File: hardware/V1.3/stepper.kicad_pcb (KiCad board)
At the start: 4 copper layers, 40 x 40 mm, 231 parts, among them J1 DRILL, J101 USB-MINI-B-SMD, J102 DRILL, J103 DRILL, J104 DRILL, J105 DRILL, J2 DRILL, J3 DRILL, J4 DRILL, J401 STACK-UP-HIGH, J402 STACK-DOWN, J403 STACK-UP-HIGH, J404 STACK-DOWN, J5 USB-MINI-B-SMD, J6 STACK-UP-HIGH, J7 STACK-DOWN, J8 STACK-UP-HIGH, J9 STACK-DOWN, P1 black, P2 green, P201 black, P202 green, P3 CON-SENSOR, P301 CON-SENSOR, P302 CON-SENSOR, P4 CON-SENSOR, Q1 FDS8449, Q2 AO4421, Q201 FDS8449, Q202 AO4421, Q203 2N7002, Q3 2N7002, SW1 Reset, SW101 Reset, SW102 Erase, SW2 Erase, U1 AT91SAM3SXB, U101 AT91SAM3SXB, U102 82400152, U2 ZXCT1086, U201 ZXCT1086, U202 TMC21XX, U3 DRV8811PWP, U4 EUP3406, U501 EUP3406, X1 16Mhz, X101 16Mhz

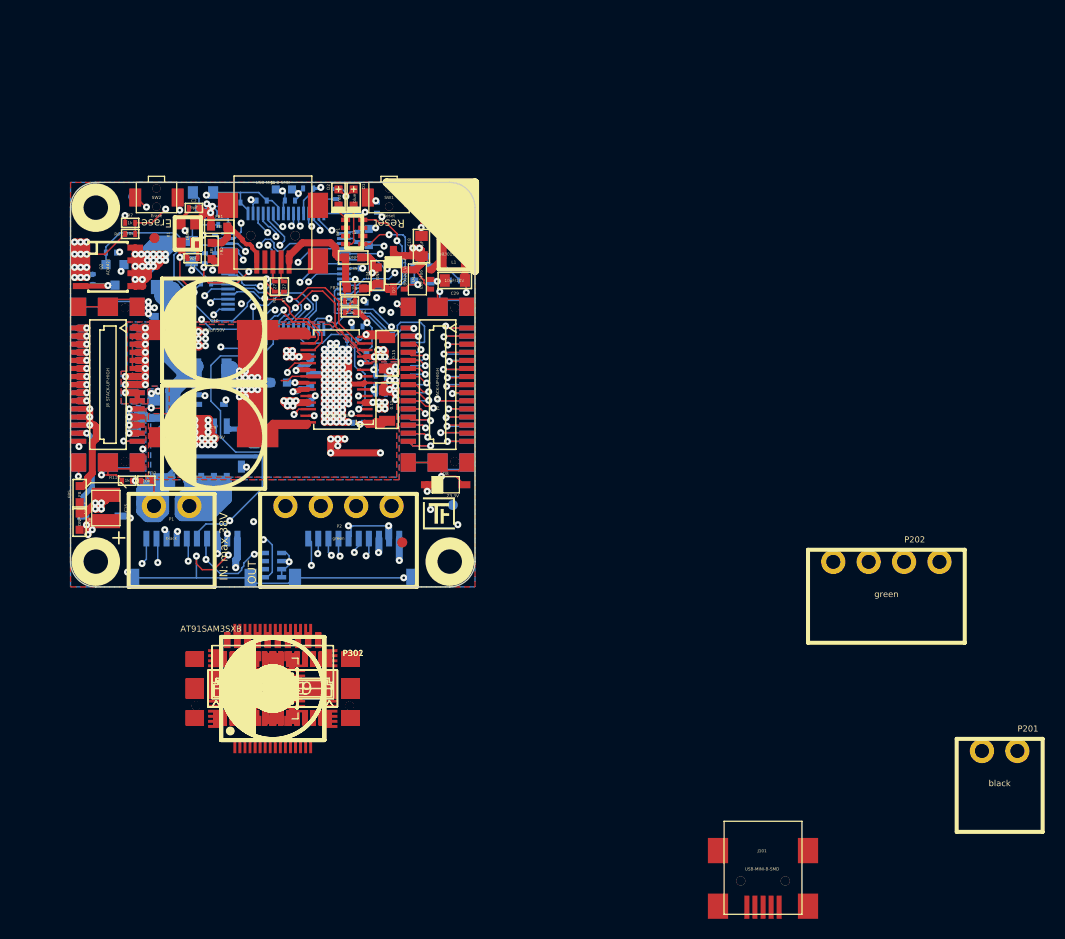
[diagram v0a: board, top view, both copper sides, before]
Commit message: remove old parts, place important components to pcb
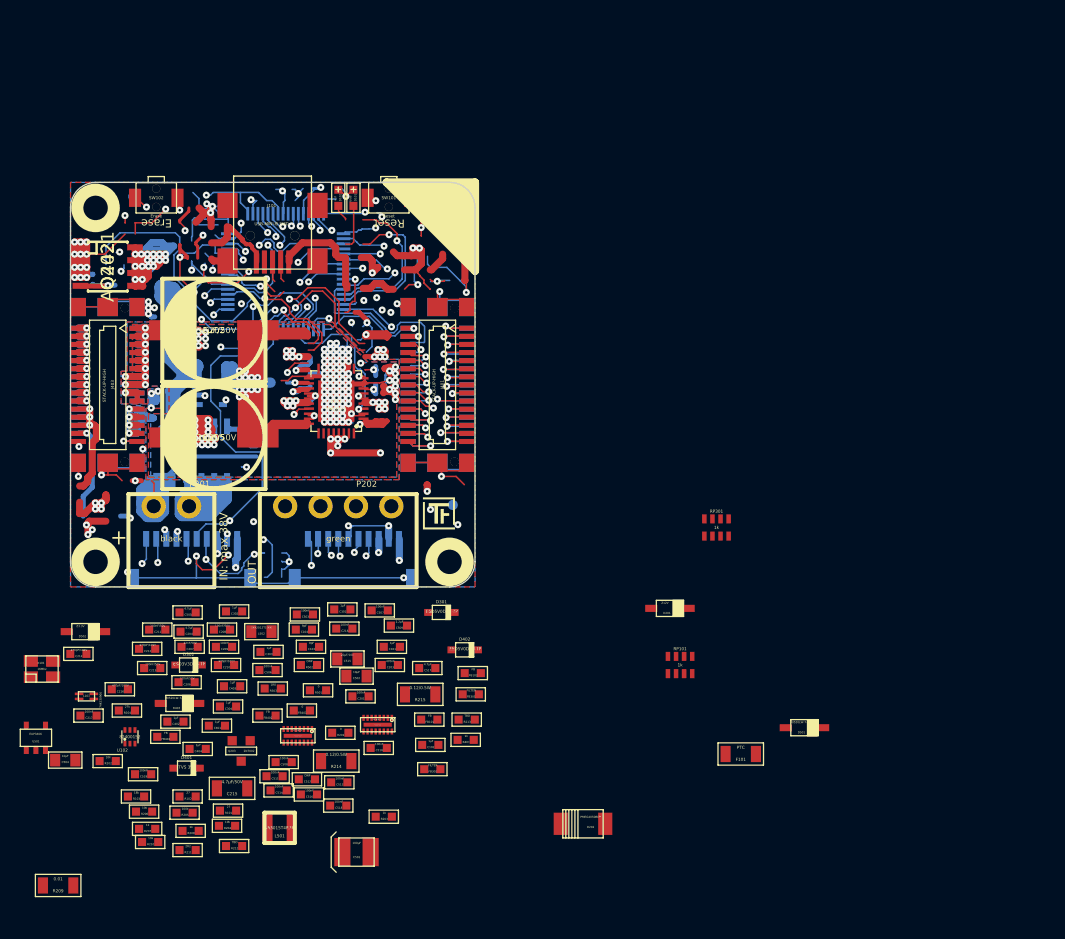
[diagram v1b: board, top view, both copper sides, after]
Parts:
- removed C1, C2: 9pF, 0402
- removed C10, C9: 330µF/50V, ELKO_103
- removed C11, C14, C17, C20, C21, C22, C24, C25, C27, C28, C3, C30, C32, C33, C4, C5: 100nF, 0402
- removed C12, C13, C7: 220nF, 0603
- removed C15: 100µF, 3528-21
- removed C16, C18: 10µF, 0805
- removed C19, C31: 4.7µF, 0603
- removed C23: 2.2µF, 0603
- removed C26: DNP, 0402
- removed C29: 10µF/10V, 0805
- removed C34, C35, C36, R24: DNP, 0603
- removed C6, C8: 1nF, 0402
- removed D1: blue, D0603
- removed D2: red, D0603
- removed D3: Z12V, SOD-123
- removed D4, D5: PMEG4050BEP, SOD-128
- removed D6, D7: B0520LW-7-F, SOD-123
- removed D8: Z3.3V, SOD-123
- removed FB1, FB2, FB3, FB4, FB5, R5: FB, 0603
- removed the Fiducial_Mark at (135.0, 78.3)
- removed the Fiducial_Mark at (159.5, 108.4)
- removed J1, J2, J3, J4: DRILL, DRILL_NP
- removed J5: USB-MINI-B-SMD, USB-MINI-B-SMD
- removed J6, J8: STACK-UP-HIGH, BTB08-ACS-TOP
- removed J7, J9: STACK-DOWN, BTB08-ACS-BTM
- removed L1: NR3015T4R7M, NR3030
- removed L2: LBR2012T100K, 0805
- removed P1: black, OQ_2P
- removed P2: green, OQ_4P
- removed P3, P4: CON-SENSOR, CON-SENSOR
- removed Q1: FDS8449, SOIC-8-MOSFET
- removed Q2: AO4421, SOIC-8-MOSFET
- removed Q3: 2N7002, SOT23GDS
- removed R1, R2: 27, 0402
- removed R10, R12, R18, R6, R8: 10k, 0402
- removed R11, R13, R16, R22, R7: 1k, 0402
- removed R14, R4: 2.7k, 0402
- removed R15, R19: 47k, 0402
- removed R17: 0.01, 1206
- removed R20, R21: 0.15, 1206
- removed R23: 0, 0603
- removed R25: 1R0, 0402
- removed R3: 1.8k, 0402
- removed R9: 100k, 0402
- removed RP1, RP2: 1k, 4X0603
- removed SW1: Reset, TACT-SWITCH
- removed SW2: Erase, TACT-SWITCH
- removed U1: AT91SAM3SXB, LQFP64
- removed U2: ZXCT1086, SOT23-5
- removed U3: DRV8811PWP, HTSSOP28
- removed U4: EUP3406, SOT23-5
- removed X1: 16Mhz, CRYSTAL_3225
- C103, C104, C503, C506, C507, C508, C510, C511, C512, C513, C514, C516, C518, C519, R101, R102, R103, R104, R202, R203, R204, R205, R206, R207, R208, R210, R211, R212, R213, R401, R503: footprint kicad-libraries:0402 -> kicad-libraries:0603
- D203, J402, J404, P301, P302, Q201, U101, U201: moved to B.Cu
- moved P201 85.4 mm to (136.7, 104.8)
- moved J101 80.1 mm to (146.7, 72.8)
- moved P202 54.5 mm to (153.2, 104.8)
- moved D501 52.7 mm to (199.3, 126.7)
- moved J104 50.7 mm to (129.2, 75.3)
- moved J103 50.6 mm to (164.2, 75.3)
- moved SW102 49.9 mm to (135.2, 74.3)
- moved SW101 49.9 mm to (158.2, 74.3)
- moved D101 49.2 mm to (154.7, 74.3), turned to 270 degrees
- moved D102 49.0 mm to (153.2, 74.3), turned to 270 degrees
- moved F101 46.7 mm to (193.0, 129.3)
- moved RP301 46.7 mm to (190.6, 106.9)
- moved Q202 44.8 mm to (130.4, 81.1), turned to 270 degrees
- moved U101 41.2 mm to (148.0, 81.6)
- moved RP101 40.3 mm to (187.0, 120.5)
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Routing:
- net VSTACK: track 99.9 -> 0.00 mm, vias 8 -> 0
- net Net-(C303-Pad1): track 0.00 -> 99.9 mm, vias 0 -> 8
- net N-000105: track 87.2 -> 0.00 mm, vias 5 -> 0
- net Net-(C212-Pad2): track 0.00 -> 87.2 mm, vias 0 -> 5
- net VPP: track 78.3 -> 0.00 mm, vias 16 -> 0
- net Net-(C202-Pad1): track 0.00 -> 78.3 mm, vias 0 -> 16
- net Net-(C210-Pad2): track 0.00 -> 74.5 mm, vias 0 -> 5
- net N-000108: track 74.5 -> 0.00 mm, vias 5 -> 0
- net (no net): track 0.00 -> 71.9 mm, vias 0 -> 14
- net Net-(FILTER302-Pad7): track 0.00 -> 62.1 mm, vias 0 -> 1
- net BRICKLET-IO1_3: track 75.9 -> 13.8 mm, vias 2 -> 1
- net Net-(C214-Pad2): track 0.00 -> 61.8 mm, vias 0 -> 5
- net N-000100: track 61.8 -> 0.00 mm, vias 5 -> 0
- net BRICKLET-I2C-SCL: track 83.6 -> 23.6 mm, vias 4 -> 2
- net Net-(FILTER301-Pad1): track 0.00 -> 57.3 mm, vias 0 -> 1
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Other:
- board text added: "1.3"
- board text removed: "1.2"

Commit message: change step down to ldo, pcb: partially placement
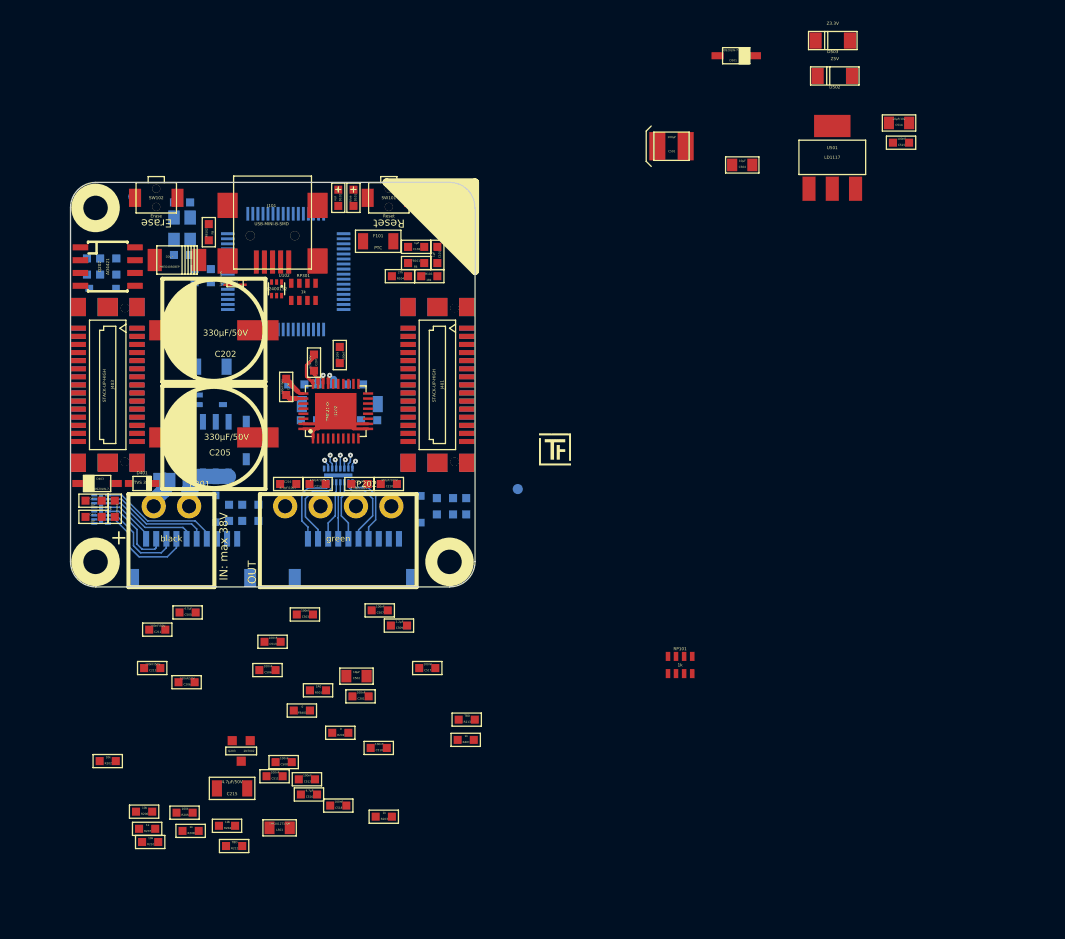
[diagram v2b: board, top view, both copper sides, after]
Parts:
- removed C519: 100nF, kicad-libraries:0603
- removed L502: LBR2012T100K, kicad-libraries:0805
- removed R502: DNP, kicad-libraries:0603
- removed R503: 1R0, kicad-libraries:0603
- added D503: Z3.3V, kicad-libraries:MiniMelf, F.Cu at (202.1, 58.8)
- C103, C104, C203, C204, C217, C218, C301, C302, C303, C304, C402, C404, D201, D301, D302, D402, FB301, FB302, FB403, FILTER301, FILTER302, R101, R102, R209, R211, R214, R215, X101: moved to B.Cu
- C512: value DNP -> 100nF
- C514: value 100nF -> 10µF/10V; footprint kicad-libraries:0603 -> kicad-libraries:0805
- C515: value 10µF/10V -> 100nF; footprint kicad-libraries:0805 -> kicad-libraries:0603
- C516: value 100nF -> 4.7µF
- C517: value 4.7µF -> 100nF
- D502: value Z3.3V -> Z5V; footprint kicad-libraries:SOD-123 -> kicad-libraries:MiniMelf
- L501: value NR3015T4R7M -> LBR2012T100K; footprint kicad-libraries:NR3030 -> kicad-libraries:0805
- R501: value 0 -> 1R0
- U501: value EUP3406 -> LD1117; footprint kicad-libraries:SOT23-5 -> kicad-libraries:SOT-223
- moved U501 97.4 mm to (202.1, 70.3)
- moved D502 92.3 mm to (202.3, 62.2)
- moved C514 90.1 mm to (208.7, 66.9)
- moved C504 89.1 mm to (193.2, 71.0)
- moved C501 76.4 mm to (186.2, 69.2)
- moved C515 74.9 mm to (208.8, 68.8)
- moved D202 68.7 mm to (137.2, 80.5), turned to 180 degrees
- moved D501 66.8 mm to (192.6, 60.2)
- moved F101 62.1 mm to (157.2, 78.6), turned to 180 degrees
- moved R103 59.1 mm to (162.2, 82.0), turned to 180 degrees
- moved R209 53.5 mm to (140.7, 91.0), turned to 180 degrees
- moved R101 52.3 mm to (139.8, 82.7)
- moved R102 52.2 mm to (139.8, 81.3)
- moved FB102 50.8 mm to (140.4, 77.7), turned to 270 degrees
- moved R104 50.7 mm to (159.3, 82.0)
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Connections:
- C512 pad 1: 3V3 -> Net-(C509-Pad1)
- C512 pad 2: Net-(C512-Pad2) -> GND
- C514 pad 1: Net-(C509-Pad1) -> 3V3
- C516 pad 1: 3V3 -> Net-(C516-Pad1)
- C518 pad 1: Net-(C518-Pad1) -> 3V3
- D502 pad 2: 3V3 -> VSTACK
- FILTER301 pad 10: BRICKLET-IO0_3 -> BRICKLET-IO0_0/AD0
- FILTER301 pad 11: BRICKLET-IO0_2/PWM0 -> BRICKLET-IO0_1
- FILTER301 pad 12: BRICKLET-IO0_1 -> BRICKLET-IO0_2/PWM0
- FILTER301 pad 13: BRICKLET-IO0_0/AD0 -> BRICKLET-IO0_3
- L501 pad 1: Net-(L501-Pad1) -> Net-(C509-Pad1)
- L501 pad 2: 3V3 -> Net-(C517-Pad1)
- P301 pad 10: Net-(FILTER301-Pad7) -> Net-(FILTER301-Pad4)
- P301 pad 7: Net-(FILTER301-Pad4) -> Net-(FILTER301-Pad7)
- P301 pad 8: Net-(FILTER301-Pad5) -> Net-(FILTER301-Pad6)
- P301 pad 9: Net-(FILTER301-Pad6) -> Net-(FILTER301-Pad5)
- R501 pad 1: 3V3 -> Net-(C516-Pad1)
- R501 pad 2: Net-(C512-Pad2) -> Net-(C517-Pad1)
- U101 pad 64: Net-(C518-Pad1) -> Net-(C517-Pad1)
- U102 pad 1: Net-(J101-Pad3) -> Net-(J101-Pad2)
- U102 pad 3: Net-(J101-Pad2) -> Net-(J101-Pad3)
- U102 pad 4: Net-(L101-Pad4) -> Net-(L101-Pad1)
- U102 pad 6: Net-(L101-Pad1) -> Net-(L101-Pad4)
- U501 pad 1: VSTACK -> GND
- U501 pad 2: GND -> 3V3
- U501 pad 3: Net-(L501-Pad1) -> VSTACK
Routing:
- net GND: track 394.0 -> 0.92 mm, vias 43 -> 1
- net STACK-PGND: track 244.2 -> 19.4 mm, vias 115 -> 0
- net 3V3: track 211.3 -> 0.00 mm, vias 13 -> 0
- net STACK-PVCC: track 118.0 -> 0.00 mm, vias 22 -> 0
- net Net-(C303-Pad1): track 99.9 -> 0.00 mm, vias 8 -> 0
- net Net-(C212-Pad2): track 87.2 -> 0.00 mm, vias 5 -> 0
- net Net-(C202-Pad1): track 78.3 -> 2.94 mm, vias 16 -> 0
- net Net-(C210-Pad2): track 74.5 -> 0.00 mm, vias 5 -> 0
- net (no net): track 71.9 -> 0.00 mm, vias 14 -> 0
- net Net-(C214-Pad2): track 61.8 -> 0.00 mm, vias 5 -> 0
- net Net-(C216-Pad2): track 54.5 -> 0.00 mm, vias 5 -> 0
- net Net-(FILTER302-Pad7): track 62.1 -> 8.01 mm, vias 1 -> 0
- net Net-(C509-Pad1): track 53.6 -> 0.00 mm, vias 4 -> 0
- net Net-(FILTER302-Pad6): track 54.2 -> 8.12 mm, vias 1 -> 0
- net Net-(FILTER301-Pad1): track 57.3 -> 11.9 mm, vias 1 -> 0
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- removed copper zone on VCC, net 3V3
- removed copper zone on B.Cu, net GND
- removed copper zone on F.Cu, net GND
- removed copper zone on GND, net GND
- removed copper zone on B.Cu, net STACK-PGND
- removed copper zone on F.Cu, net STACK-PGND
- removed copper zone on GND, net STACK-PGND
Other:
- net class Default: via_dia 0.70104 -> 0.5; via_drill 0.24892 -> 0.15
- rule via_min_drill: 0.24892 -> 0.15
- rule via_min_size: 0.70104 -> 0.5

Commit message: placement finished
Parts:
- removed FB403: FB, kicad-libraries:0603
- C201, C215, C502, C503, C504, C505, C506, C507, C508, C509, C510, C511, C512, C513, C514, C515, C516, C517, C518, D503, FB402, L501, Q203, R201, R202, R203, R205, R206, R207, R208, R210, R501, RP101, U501: moved to B.Cu
- FB401: value 0 -> FB
- R101, R102: moved to F.Cu
- moved R203 62.3 mm to (133.9, 78.0), turned to 180 degrees
- moved L501 61.3 mm to (140.6, 75.7), turned to 270 degrees
- moved C518 60.9 mm to (142.0, 74.5), turned to 90 degrees
- moved C516 60.7 mm to (139.9, 73.5)
- moved R204 59.0 mm to (133.9, 78.0), turned to 180 degrees
- moved C511 57.2 mm to (149.5, 74.3), turned to 90 degrees
- moved RP101 56.5 mm to (153.9, 74.7), turned to 180 degrees
- moved C510 54.4 mm to (147.3, 75.2)
- moved R208 54.1 mm to (134.2, 83.0)
- moved R202 53.5 mm to (133.9, 76.7)
- moved C515 50.5 mm to (158.9, 76.3)
- moved R212 50.4 mm to (154.3, 89.3), turned to 90 degrees
- moved Q203 49.4 mm to (134.1, 80.5)
- moved C502 49.1 mm to (144.2, 73.7), turned to 180 degrees
- moved C508 49.1 mm to (137.8, 82.0), turned to 180 degrees
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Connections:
- FB401 pad 1: Net-(FB401-Pad1) -> 3V3
- FB401 pad 2: GND -> Net-(C403-Pad1)
- FB402 pad 1: 3V3 -> VSTACK
- FB402 pad 2: Net-(C403-Pad1) -> Net-(C404-Pad1)
- J403 pad 21: Net-(FB401-Pad1) -> GND
- J403 pad 23: Net-(FB401-Pad1) -> GND
- J403 pad 25: Net-(FB401-Pad1) -> GND
- J403 pad 27: Net-(FB401-Pad1) -> GND
- J404 pad 21: Net-(FB401-Pad1) -> GND
- J404 pad 23: Net-(FB401-Pad1) -> GND
- J404 pad 25: Net-(FB401-Pad1) -> GND
- J404 pad 27: Net-(FB401-Pad1) -> GND
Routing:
- net Net-(D202-Pad2): track 0.00 -> 8.10 mm
- net Net-(C509-Pad1): track 0.00 -> 6.01 mm
- net Net-(C209-Pad2): track 0.00 -> 2.68 mm
- net 3V3: track 0.00 -> 2.11 mm

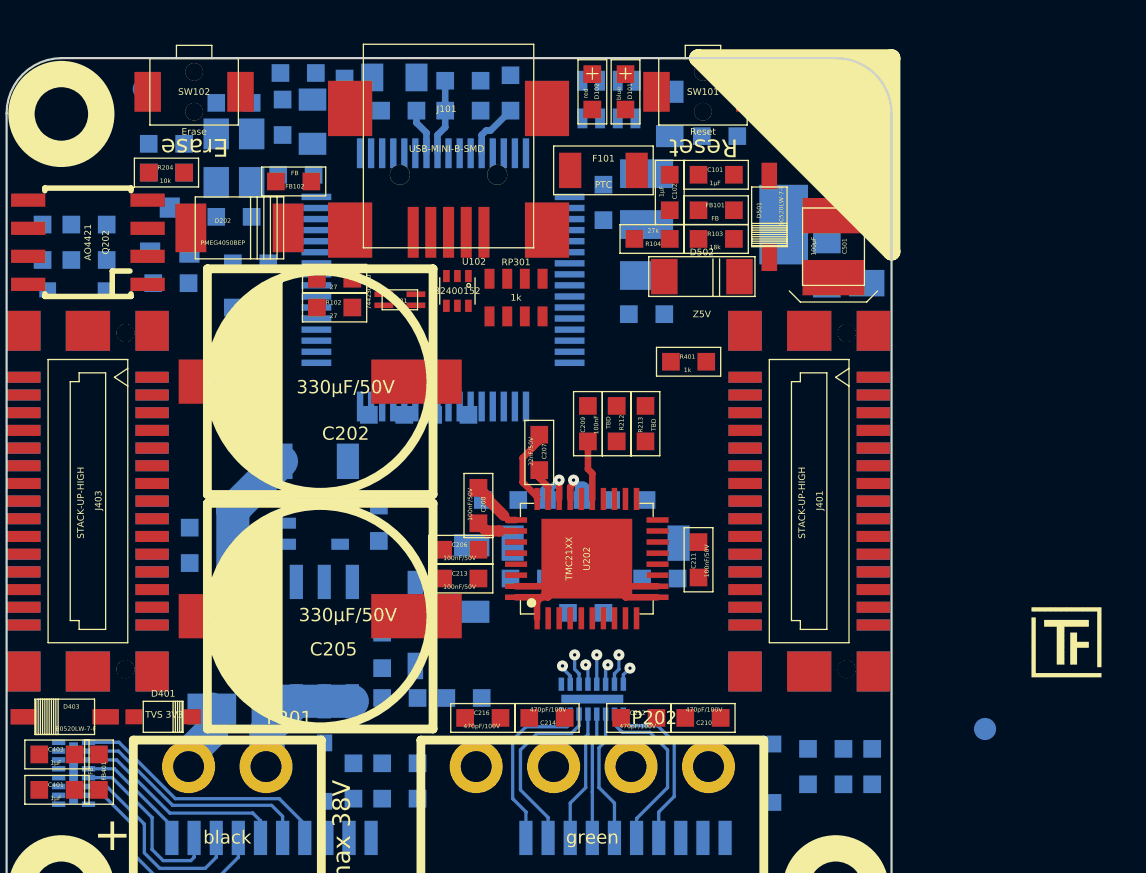
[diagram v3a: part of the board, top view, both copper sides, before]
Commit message: previous commit was uncomplete. parts placement finished
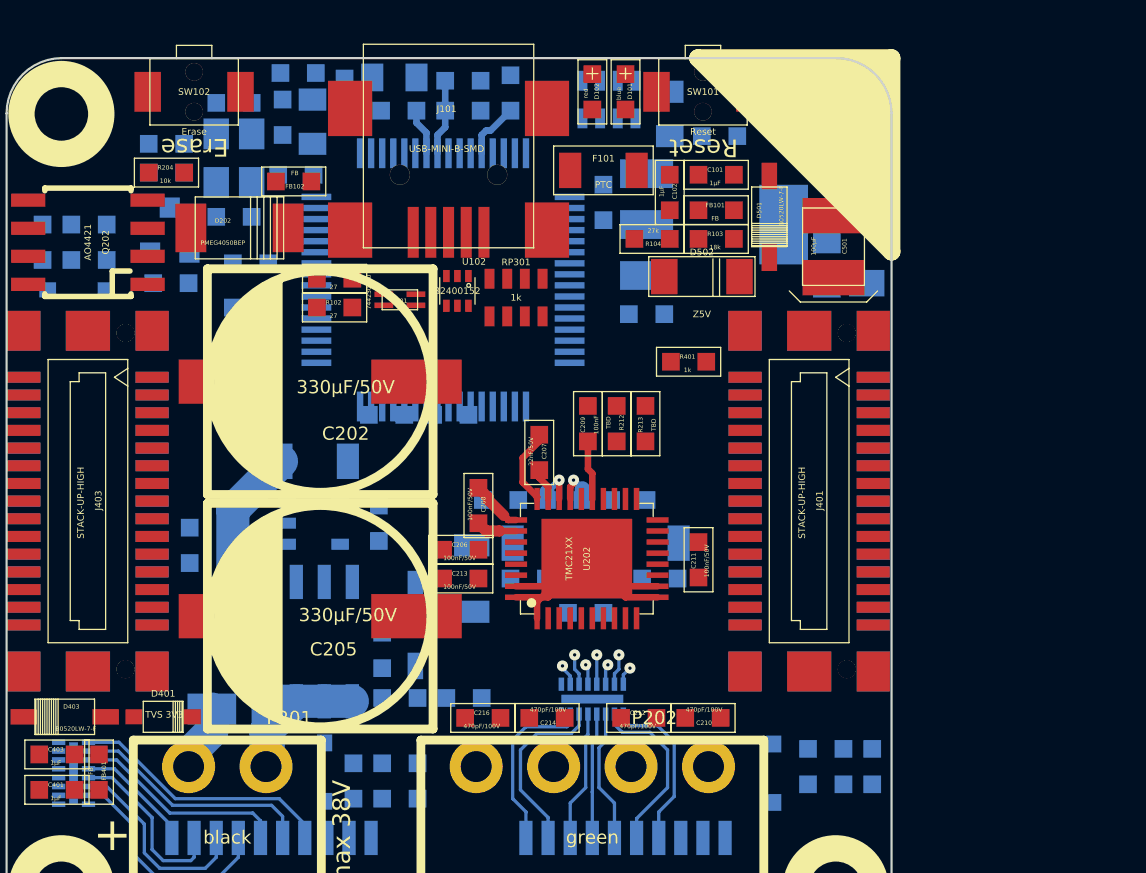
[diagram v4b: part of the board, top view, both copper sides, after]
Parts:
- removed Fiducial_Mark (x2): VAL**, Fiducial_Mark
- removed G***: Logo_31x31, Logo_31x31
- removed VAL: WEEE_7mm, WEEE_7mm
- removed VAL: CE_5mm, CE_5mm
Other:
- board text removed: "tinkerforge.com"
